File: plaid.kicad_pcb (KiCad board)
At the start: 2 copper layers, 228 x 98 mm, 139 parts, among them J1 USB_OTG, J2 AVR_ISP_6, J3 Conn_01x04, J4 GS2, J5 GS2, SW1 SW_Push, SW10 SW_Push, SW11 SW_Push, SW12 SW_Push, SW13 SW_Push, SW14 SW_Push, SW15 SW_Push, SW16 SW_Push, SW17 SW_Push, SW18 SW_Push, SW19 SW_Push, SW2 SW_Push, SW20 SW_Push, SW21 SW_Push, SW22 SW_Push, SW23 SW_Push, SW24 SW_Push, SW25 SW_Push, SW26 SW_Push, SW27 SW_Push, SW28 SW_Push, SW29 SW_Push, SW3 SW_Push, SW30 SW_Push, SW31 SW_Push, SW32 SW_Push, SW33 SW_Push, SW34 SW_Push, SW35 SW_Push, SW36 SW_Push, SW37 SW_Push, SW38 SW_Push, SW39 SW_Push, SW4 SW_Push, SW40 SW_Push, SW41 SW_Push, SW42 SW_Push, SW43 SW_Push, SW44 SW_Push, SW45 SW_Push, SW46 SW_Push, SW47 SW_Push, SW48 SW_Push, SW49 SW_Push, SW5 SW_Push, SW50 RESET, SW51 BOOT, SW6 SW_Push, SW7 SW_Push, SW8 SW_Push, SW9 SW_Push, U1 ATMEGA328-PU, Y1 16MHz

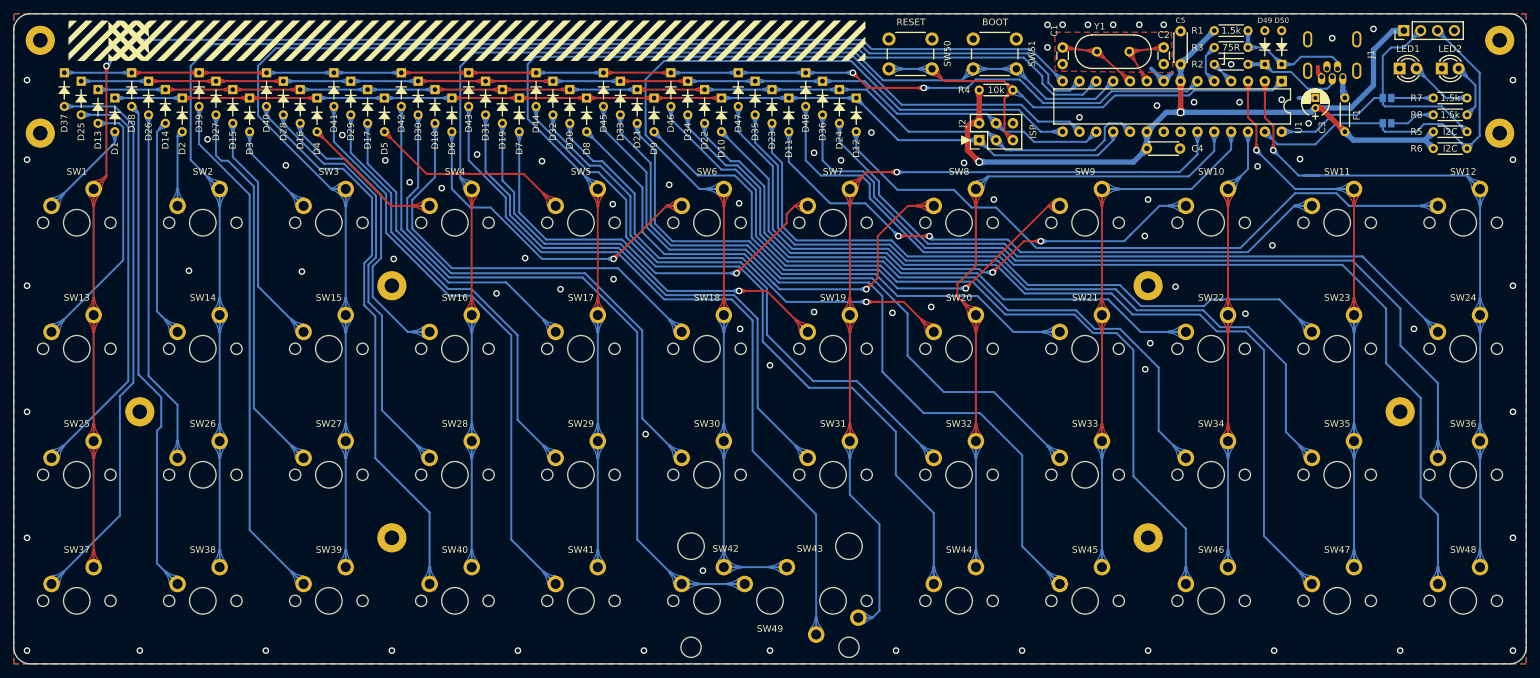
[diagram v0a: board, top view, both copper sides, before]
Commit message: Update PCB to new KiCAD
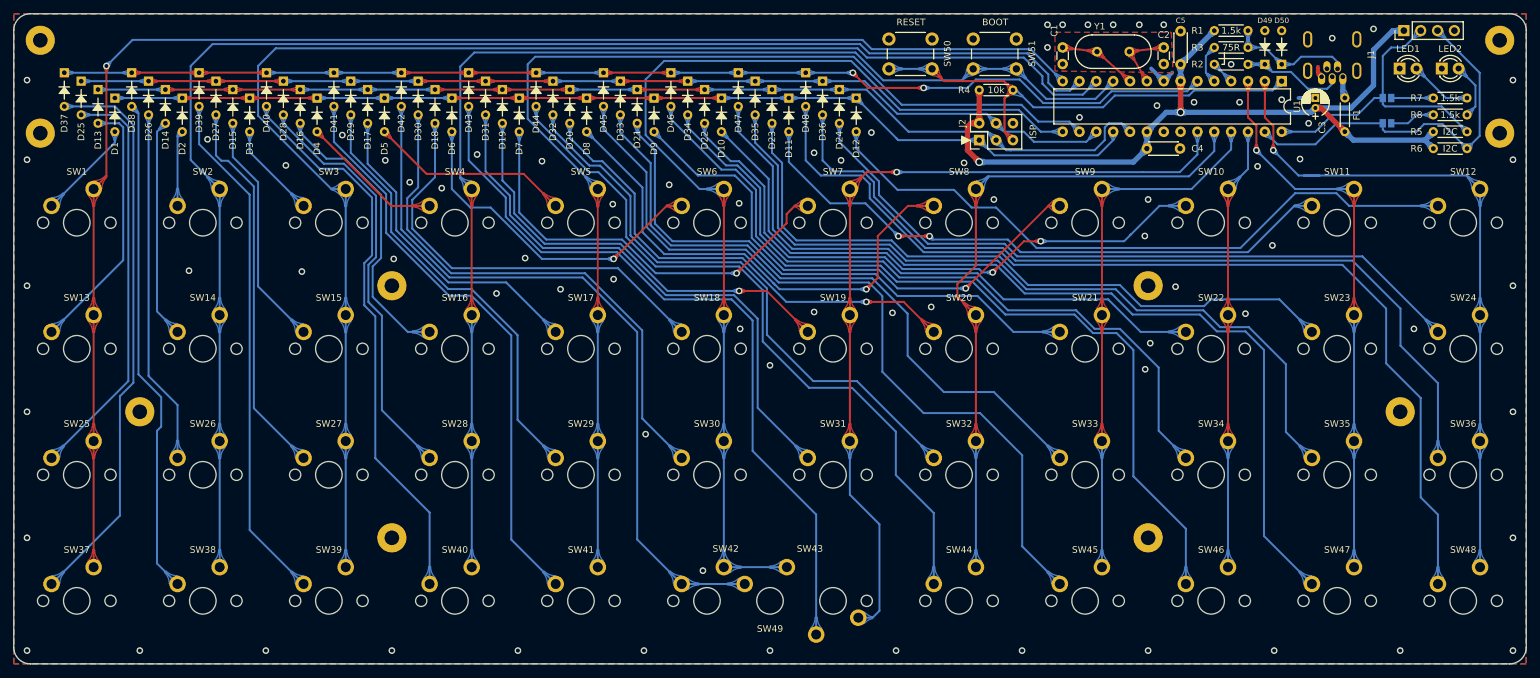
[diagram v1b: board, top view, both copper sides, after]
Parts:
- removed G***: LOGO, plaid_silk:plaid_silk
- removed G***: LOGO, dm9_silks:logo_hsgw_7_5mm
- removed G***: LOGO, dm9_silks:logo_dm9_15mm
- removed G***: LOGO, plaid_silk:plaid_katakana
- removed REF**: Stab_MX_2u, SMKJP:Stab_MX_2u
- C3: value 10u -> 4.7u
- U1: footprint Housings_DIP:DIP-28_W7.62mm -> Package_DIP:DIP-28_W7.62mm
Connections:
- D1 pad 1: /ROW0 -> unconnected-(D1-Pad1)
- D10 pad 1: /ROW0 -> unconnected-(D10-Pad1)
- D11 pad 1: /ROW0 -> unconnected-(D11-Pad1)
- D13 pad 1: /ROW1 -> unconnected-(D13-Pad1)
- D14 pad 1: /ROW1 -> unconnected-(D14-Pad1)
- D15 pad 1: /ROW1 -> unconnected-(D15-Pad1)
- D16 pad 1: /ROW1 -> unconnected-(D16-Pad1)
- D17 pad 1: /ROW1 -> unconnected-(D17-Pad1)
- D18 pad 1: /ROW1 -> unconnected-(D18-Pad1)
- D19 pad 1: /ROW1 -> unconnected-(D19-Pad1)
- D2 pad 1: /ROW0 -> unconnected-(D2-Pad1)
- D20 pad 1: /ROW1 -> unconnected-(D20-Pad1)
- D21 pad 1: /ROW1 -> unconnected-(D21-Pad1)
- D22 pad 1: /ROW1 -> unconnected-(D22-Pad1)
- D23 pad 1: /ROW1 -> unconnected-(D23-Pad1)
- D25 pad 1: /ROW2 -> unconnected-(D25-Pad1)
- D26 pad 1: /ROW2 -> unconnected-(D26-Pad1)
- D27 pad 1: /ROW2 -> unconnected-(D27-Pad1)
- D28 pad 1: /ROW2 -> unconnected-(D28-Pad1)
- D29 pad 1: /ROW2 -> unconnected-(D29-Pad1)
- D3 pad 1: /ROW0 -> unconnected-(D3-Pad1)
- D30 pad 1: /ROW2 -> unconnected-(D30-Pad1)
- D31 pad 1: /ROW2 -> unconnected-(D31-Pad1)
- D32 pad 1: /ROW2 -> unconnected-(D32-Pad1)
- D33 pad 1: /ROW2 -> unconnected-(D33-Pad1)
- D34 pad 1: /ROW2 -> unconnected-(D34-Pad1)
- D35 pad 1: /ROW2 -> unconnected-(D35-Pad1)
- D37 pad 1: /ROW3 -> unconnected-(D37-Pad1)
- D38 pad 1: /ROW3 -> unconnected-(D38-Pad1)
- D39 pad 1: /ROW3 -> unconnected-(D39-Pad1)
- D4 pad 1: /ROW0 -> unconnected-(D4-Pad1)
- D40 pad 1: /ROW3 -> unconnected-(D40-Pad1)
- D41 pad 1: /ROW3 -> unconnected-(D41-Pad1)
- D43 pad 1: /ROW3 -> unconnected-(D43-Pad1)
- D44 pad 1: /ROW3 -> unconnected-(D44-Pad1)
- D45 pad 1: /ROW3 -> unconnected-(D45-Pad1)
- D46 pad 1: /ROW3 -> unconnected-(D46-Pad1)
- D47 pad 1: /ROW3 -> unconnected-(D47-Pad1)
- D5 pad 1: /ROW0 -> unconnected-(D5-Pad1)
- D6 pad 1: /ROW0 -> unconnected-(D6-Pad1)
- D7 pad 1: /ROW0 -> unconnected-(D7-Pad1)
- D8 pad 1: /ROW0 -> unconnected-(D8-Pad1)
- D9 pad 1: /ROW0 -> unconnected-(D9-Pad1)
- J1 pad 4: (no net) -> unconnected-(J1-Pad4)
- J1 pad 6: (no net) -> unconnected-(J1-Pad6)
- U1 pad 21: (no net) -> unconnected-(U1-Pad21)
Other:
- net class Default removed
- net class Power removed

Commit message: Start turning Plaid into Squeezebar
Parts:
- removed D37, D38, D39, D40, D41, D42, D43, D44, D45, D46, D47, D48: 1N4148, dm9_rc:D_DO-35_SOD27_P5.08mm_Horizontal
- removed H10, H3, H4, H5, H6, H7, H8, H9: M2, Mounting_Holes:MountingHole_2.2mm_M2_Pad
- removed LED1: RED, LEDs:LED_D3.0mm
- removed LED2: GREEN, LEDs:LED_D3.0mm
- removed R7, R8: 1.5k, Resistors_THT:R_Axial_DIN0204_L3.6mm_D1.6mm_P5.08mm_Horizontal
- removed SW1, SW10, SW11, SW12, SW13, SW14, SW15, SW16, SW17, SW18, SW19, SW2, SW20, SW21, SW22, SW23, SW24, SW25, SW26, SW27, SW28, SW29, SW3, SW30, SW31, SW32, SW33, SW34, SW35, SW36, SW37, SW38, SW39, SW4, SW40, SW41, SW42, SW43, SW44, SW45, SW46, SW47, SW48, SW5, SW6, SW7, SW8, SW9: SW_Push, SMKJP:SW_Cherry_MX1A_1.00u_PCB
- removed SW49: SW_Push, SMKJP:SW_Cherry_MX1A_2.0U_PCB_universal_center
- added J0: OUTR, Connector_JST:JST_PH_B5B-PH-K_1x05_P2.00mm_Vertical, F.Cu at (168.1, 47.5)
- added J1: PNK, Connector_JST:JST_PH_B5B-PH-K_1x05_P2.00mm_Vertical, F.Cu at (175.7, 47.5)
- added J10: I2C, Connector_JST:JST_PH_B5B-PH-K_1x05_P2.00mm_Vertical, F.Cu at (244.3, 47.5)
- added J13: AudioJack4, Connector_Audio:Jack_3.5mm_PJ320E_Horizontal, F.Cu at (304.3, 15.7)
- added J14: RGB, Connector_PinSocket_2.54mm:PinSocket_1x03_P2.54mm_Vertical, F.Cu at (325.0, 60.6)
- added J2: RNG, Connector_JST:JST_PH_B5B-PH-K_1x05_P2.00mm_Vertical, F.Cu at (183.3, 47.5)
- added J3: MID, Connector_JST:JST_PH_B5B-PH-K_1x05_P2.00mm_Vertical, F.Cu at (191.0, 47.5)
- added J6: THM1, Connector_JST:JST_PH_B5B-PH-K_1x05_P2.00mm_Vertical, F.Cu at (213.8, 47.5)
- added J7: THM2, Connector_JST:JST_PH_B5B-PH-K_1x05_P2.00mm_Vertical, F.Cu at (221.4, 47.5)
- added J8: ENC, Connector_JST:JST_PH_B5B-PH-K_1x05_P2.00mm_Vertical, F.Cu at (229.1, 47.5)
- added J9: I2C, Connector_JST:JST_PH_B5B-PH-K_1x05_P2.00mm_Vertical, F.Cu at (236.7, 47.5)
- added JP1: A0, Jumper:SolderJumper-3_P1.3mm_Bridged12_Pad1.0x1.5mm, F.Cu at (312.0, 71.1)
- added JP2: A1, Jumper:SolderJumper-3_P1.3mm_Bridged12_Pad1.0x1.5mm, F.Cu at (300.7, 71.0)
- added JP3: A2, Jumper:SolderJumper-3_P1.3mm_Bridged12_Pad1.0x1.5mm, F.Cu at (306.3, 71.1)
- added U2: MCP23017_SP, Package_DIP:DIP-28_W7.62mm, F.Cu at (264.6, 28.4)
- D33, D34, D35, D36: value 1N4148 -> WS2812B; footprint dm9_rc:D_DO-35_SOD27_P5.08mm_Horizontal -> LED_SMD:LED_WS2812B_PLCC4_5.0x5.0mm_P3.2mm
- H1, H2: value M2 -> M3; footprint Mounting_Holes:MountingHole_2.2mm_M2_Pad -> MountingHole:MountingHole_3.2mm_M3
- J4: value GS2 -> IDX; footprint Connectors:GS2 -> Connector_JST:JST_PH_B5B-PH-K_1x05_P2.00mm_Vertical; moved to F.Cu
- J5: value GS2 -> INNR; footprint Connectors:GS2 -> Connector_JST:JST_PH_B5B-PH-K_1x05_P2.00mm_Vertical; moved to F.Cu
- moved H1 218.7 mm to (272.2, 39.8)
- moved D33 199.5 mm to (340.8, 55.1), turned to 0 degrees
- moved D34 189.8 mm to (340.8, 48.5), turned to 0 degrees
- moved D36 185.9 mm to (356.7, 41.9), turned to 0 degrees
- moved D35 169.7 mm to (331.5, 61.6), turned to 0 degrees
- moved H2 122.4 mm to (169.4, 27.1)
- moved D1 117.7 mm to (177.0, 28.4)
- moved D2 110.0 mm to (179.5, 29.7)
- moved D3 102.4 mm to (182.1, 30.9)
- moved D4 87.5 mm to (174.5, 27.1)
- moved J4 60.4 mm to (198.6, 47.5)
- moved J5 54.3 mm to (206.2, 47.5)
- moved U1 41.6 mm to (264.6, 25.9)
- moved J15 35.7 mm to (272.2, 32.6)
- moved C4 28.6 mm to (249.4, 71.6)
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- renumbered J3 to J11, J2 to J12, J1 to J15
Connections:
- D1 pad 1: unconnected-(D1-Pad1) -> Net-(D1-Pad1)
- D1 pad 2: Net-(D1-Pad2) -> /ROW0
- D10 pad 1: unconnected-(D10-Pad1) -> Net-(D10-Pad1)
- D10 pad 2: Net-(D10-Pad2) -> /ROW1
- D11 pad 1: unconnected-(D11-Pad1) -> Net-(D11-Pad1)
- D11 pad 2: Net-(D11-Pad2) -> /ROW2
- D12 pad 1: /ROW0 -> Net-(D12-Pad1)
- D12 pad 2: Net-(D12-Pad2) -> /ROW3
- D13 pad 1: unconnected-(D13-Pad1) -> Net-(D13-Pad1)
- D13 pad 2: Net-(D13-Pad2) -> /ROW0
- D14 pad 1: unconnected-(D14-Pad1) -> Net-(D14-Pad1)
- D14 pad 2: Net-(D14-Pad2) -> /ROW1
- D15 pad 1: unconnected-(D15-Pad1) -> Net-(D15-Pad1)
- D15 pad 2: Net-(D15-Pad2) -> /ROW2
- D16 pad 1: unconnected-(D16-Pad1) -> Net-(D16-Pad1)
- D16 pad 2: Net-(D16-Pad2) -> /ROW3
- D17 pad 1: unconnected-(D17-Pad1) -> Net-(D17-Pad1)
- D17 pad 2: Net-(D17-Pad2) -> /ROW0
- D18 pad 1: unconnected-(D18-Pad1) -> Net-(D18-Pad1)
- D18 pad 2: Net-(D18-Pad2) -> /ROW1
- D19 pad 1: unconnected-(D19-Pad1) -> Net-(D19-Pad1)
- D19 pad 2: Net-(D19-Pad2) -> /ROW2
- D2 pad 1: unconnected-(D2-Pad1) -> Net-(D2-Pad1)
- D2 pad 2: Net-(D2-Pad2) -> /ROW1
- D20 pad 1: unconnected-(D20-Pad1) -> Net-(D20-Pad1)
- D20 pad 2: Net-(D20-Pad2) -> /ROW3
- D21 pad 1: unconnected-(D21-Pad1) -> Net-(D21-Pad1)
- D21 pad 2: Net-(D21-Pad2) -> /ROW0
- D22 pad 1: unconnected-(D22-Pad1) -> Net-(D22-Pad1)
- D22 pad 2: Net-(D22-Pad2) -> /ROW1
- D23 pad 1: unconnected-(D23-Pad1) -> Net-(D23-Pad1)
- D23 pad 2: Net-(D23-Pad2) -> /ROW2
- D24 pad 1: /ROW1 -> Net-(D24-Pad1)
- D24 pad 2: Net-(D24-Pad2) -> /ROW3
- D25 pad 1: unconnected-(D25-Pad1) -> Net-(D25-Pad1)
- D25 pad 2: Net-(D25-Pad2) -> /ROW0
- D26 pad 1: unconnected-(D26-Pad1) -> Net-(D26-Pad1)
- D26 pad 2: Net-(D26-Pad2) -> /ROW1
- D27 pad 1: unconnected-(D27-Pad1) -> Net-(D27-Pad1)
- D27 pad 2: Net-(D27-Pad2) -> /ROW2
- D28 pad 1: unconnected-(D28-Pad1) -> Net-(D28-Pad1)
- D28 pad 2: Net-(D28-Pad2) -> /ROW3
- D29 pad 1: unconnected-(D29-Pad1) -> Net-(D29-Pad1)
- D29 pad 2: Net-(D29-Pad2) -> /ROW0
- D3 pad 1: unconnected-(D3-Pad1) -> Net-(D3-Pad1)
- D3 pad 2: Net-(D3-Pad2) -> /ROW2
- D30 pad 1: unconnected-(D30-Pad1) -> Net-(D30-Pad1)
- D30 pad 2: Net-(D30-Pad2) -> /ROW1
- D31 pad 1: unconnected-(D31-Pad1) -> Net-(D31-Pad1)
- D31 pad 2: Net-(D31-Pad2) -> /ROW2
- D32 pad 1: unconnected-(D32-Pad1) -> Net-(D32-Pad1)
- D32 pad 2: Net-(D32-Pad2) -> /ROW3
- D33 pad 1: unconnected-(D33-Pad1) -> +5V
- D33 pad 2: Net-(D33-Pad2) -> unconnected-(D33-Pad2)
- D34 pad 1: unconnected-(D34-Pad1) -> +5V
- D34 pad 2: Net-(D34-Pad2) -> unconnected-(D34-Pad2)
- D35 pad 1: unconnected-(D35-Pad1) -> +5V
- D35 pad 2: Net-(D35-Pad2) -> unconnected-(D35-Pad2)
- D36 pad 1: /ROW2 -> +5V
- D36 pad 2: Net-(D36-Pad2) -> /RGB_OUT
- D4 pad 1: unconnected-(D4-Pad1) -> Net-(D4-Pad1)
- D4 pad 2: Net-(D4-Pad2) -> /ROW3
- D5 pad 1: unconnected-(D5-Pad1) -> Net-(D5-Pad1)
- D5 pad 2: Net-(D5-Pad2) -> /ROW0
- D6 pad 1: unconnected-(D6-Pad1) -> Net-(D6-Pad1)
- D6 pad 2: Net-(D6-Pad2) -> /ROW1
- D7 pad 1: unconnected-(D7-Pad1) -> Net-(D7-Pad1)
- D7 pad 2: Net-(D7-Pad2) -> /ROW2
- D8 pad 1: unconnected-(D8-Pad1) -> Net-(D8-Pad1)
- D8 pad 2: Net-(D8-Pad2) -> /ROW3
- D9 pad 1: unconnected-(D9-Pad1) -> Net-(D9-Pad1)
- D9 pad 2: Net-(D9-Pad2) -> /ROW0
- J12 pad 1: /ROW0 -> /ROW2
- J12 pad 4: /ROW2 -> /ROW3
- J4 pad 1: Net-(J4-Pad1) -> /COL4
- J4 pad 2: /i2c_SCL -> Net-(D17-Pad1)
- J5 pad 1: Net-(J5-Pad1) -> /COL5
- J5 pad 2: /i2c_SDA -> Net-(D21-Pad1)
- SW51 pad 1: /COL3 -> /BOOT
- U1 pad 11: /COL3 -> /BOOT
- U1 pad 17: /ROW2 -> /ROW3
- U1 pad 18: /ROW0 -> /ROW2
- U1 pad 2: /COL11 -> /ROW0
- U1 pad 25: /COL8 -> /E1
- U1 pad 26: /COL9 -> /E2
- U1 pad 3: /COL10 -> /COL3
- U1 pad 6: /ROW3 -> /RGB
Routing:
- net /COL0: track 224.7 -> 0.00 mm, vias 1 -> 0
- net /COL1: track 217.0 -> 0.00 mm
- net /COL2: track 214.2 -> 0.00 mm
- net /COL3: track 180.9 -> 0.00 mm
- net /ROW3: track 175.6 -> 0.00 mm, vias 2 -> 0
- net /COL4: track 168.5 -> 0.00 mm
- net /ROW1: track 162.9 -> 0.00 mm
- net /COL5: track 158.5 -> 0.00 mm
- net /ROW2: track 157.5 -> 0.00 mm
- net /ROW0: track 156.3 -> 0.00 mm
- net Net-(D48-Pad2): track 150.9 -> 0.00 mm
- net Net-(D47-Pad2): track 140.5 -> 0.00 mm
- net Net-(D36-Pad2): track 129.4 -> 0.00 mm
- net Net-(D46-Pad2): track 128.7 -> 0.00 mm
- net +5V: track 127.6 -> 0.00 mm, vias 2 -> 0
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- removed copper zone on B.Cu, net GND
- removed copper zone on F.Cu, net GND
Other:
- board size 228 x 98 mm -> 110.5 x 26.7 mm

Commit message: Route a Squeezebar
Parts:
- removed D1, D10, D11, D12, D13, D14, D15, D16, D17, D18, D19, D2, D20, D21, D22, D23, D24, D25, D26, D27, D28, D29, D3, D30, D31, D32, D4, D5, D6, D7, D8, D9: 1N4148, dm9_rc:D_DO-35_SOD27_P5.08mm_Horizontal
- removed D33, D34, D35, D36: WS2812B, LED_SMD:LED_WS2812B_PLCC4_5.0x5.0mm_P3.2mm
- removed J12: AVR_ISP_6, Pin_Headers:Pin_Header_Straight_2x03_Pitch2.54mm
- removed J13: AudioJack4, Connector_Audio:Jack_3.5mm_PJ320E_Horizontal
- removed JP1: A0, Jumper:SolderJumper-3_P1.3mm_Bridged12_Pad1.0x1.5mm
- removed JP2: A1, Jumper:SolderJumper-3_P1.3mm_Bridged12_Pad1.0x1.5mm
- removed JP3: A2, Jumper:SolderJumper-3_P1.3mm_Bridged12_Pad1.0x1.5mm
- H1, H2: value M3 -> M2; footprint MountingHole:MountingHole_3.2mm_M3 -> MountingHole:MountingHole_2.2mm_M2
- moved J14 266.1 mm to (58.9, 57.1), turned to 180 degrees
- moved U1 134.0 mm to (135.1, 60.2)
- moved U2 134.0 mm to (135.1, 62.7)
- moved SW51 132.1 mm to (69.0, 56.6)
- moved J7 126.4 mm to (97.0, 69.4)
- moved J6 125.1 mm to (90.6, 69.4)
- moved R5 124.7 mm to (140.3, 51.9), turned to -90 degrees
- moved J5 123.9 mm to (84.3, 69.4)
- moved J4 122.6 mm to (77.9, 69.4)
- moved R6 122.6 mm to (142.8, 51.9), turned to -90 degrees
- moved J3 121.4 mm to (71.6, 69.4)
- moved J2 120.1 mm to (65.2, 69.4)
- moved H2 119.1 mm to (53.2, 53.2)
- moved J1 118.9 mm to (58.9, 69.4)
- moved J0 117.6 mm to (52.5, 69.4)
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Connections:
- J0 pad 2: Net-(D1-Pad1) -> /ROW0
- J0 pad 3: Net-(D2-Pad1) -> /ROW1
- J0 pad 4: Net-(D3-Pad1) -> /ROW2
- J0 pad 5: Net-(D4-Pad1) -> /ROW3
- J1 pad 2: Net-(D5-Pad1) -> /ROW0
- J1 pad 3: Net-(D6-Pad1) -> /ROW1
- J1 pad 4: Net-(D7-Pad1) -> /ROW2
- J1 pad 5: Net-(D8-Pad1) -> /ROW3
- J10 pad 2: /i2c_SDA -> /INT
- J10 pad 3: /i2c_SCL -> /i2c_SDA
- J10 pad 4: /INT -> /i2c_SCL
- J11 pad 2: /i2c_SCL -> /i2c_SDA
- J11 pad 3: /i2c_SDA -> /i2c_SCL
- J14 pad 2: /RGB_OUT -> /RGB
- J2 pad 2: Net-(D9-Pad1) -> /ROW0
- J2 pad 3: Net-(D10-Pad1) -> /ROW1
- J2 pad 4: Net-(D11-Pad1) -> /ROW2
- J2 pad 5: Net-(D12-Pad1) -> /ROW3
- J3 pad 2: Net-(D13-Pad1) -> /ROW0
- J3 pad 3: Net-(D14-Pad1) -> /ROW1
- J3 pad 4: Net-(D15-Pad1) -> /ROW2
- J3 pad 5: Net-(D16-Pad1) -> /ROW3
- J4 pad 2: Net-(D17-Pad1) -> /ROW0
- J4 pad 3: Net-(D18-Pad1) -> /ROW1
- J4 pad 4: Net-(D19-Pad1) -> /ROW2
- J4 pad 5: Net-(D20-Pad1) -> /ROW3
- J5 pad 2: Net-(D21-Pad1) -> /ROW0
- J5 pad 3: Net-(D22-Pad1) -> /ROW1
- J5 pad 4: Net-(D23-Pad1) -> /ROW2
- J5 pad 5: Net-(D24-Pad1) -> /ROW3
- J6 pad 2: Net-(D25-Pad1) -> /ROW0
- J6 pad 3: Net-(D26-Pad1) -> /ROW1
- J6 pad 4: Net-(D27-Pad1) -> /ROW2
- J6 pad 5: Net-(D28-Pad1) -> /ROW3
- J7 pad 2: Net-(D29-Pad1) -> /ROW0
- J7 pad 3: Net-(D30-Pad1) -> /ROW1
- J7 pad 4: Net-(D31-Pad1) -> /ROW2
- J7 pad 5: Net-(D32-Pad1) -> /ROW3
- J8 pad 1: GND -> /E2
- J8 pad 2: /BOOT -> GND
- J8 pad 4: GND -> /ROW3
- J8 pad 5: /E2 -> /COL0
- J9 pad 2: /i2c_SDA -> /INT
- J9 pad 3: /i2c_SCL -> /i2c_SDA
- J9 pad 4: /INT -> /i2c_SCL
- R5 pad 2: /i2c_SCL -> /i2c_SDA
- R6 pad 2: /i2c_SDA -> /i2c_SCL
- SW51 pad 1: /BOOT -> /COL0
- U1 pad 11: /BOOT -> /COL0
- U1 pad 12: /COL2 -> /COL3
- U1 pad 13: /COL1 -> /RGB
- U1 pad 14: /COL0 -> /COL7
- U1 pad 17: /ROW3 -> /INT
- U1 pad 18: /ROW2 -> /ROW0
- U1 pad 2: /ROW0 -> /COL1
- U1 pad 23: /COL6 -> /ROW2
- U1 pad 24: /COL7 -> /ROW3
- U1 pad 3: /COL3 -> /COL2
- U1 pad 6: /RGB -> /COL6
- U2 pad 15: /A2 -> +5V
- U2 pad 16: /A1 -> +5V
- U2 pad 17: /A0 -> +5V
- U2 pad 19: /INT -> unconnected-(U2-Pad19)
- U2 pad 20: unconnected-(U2-Pad20) -> /INT
- U2 pad 28: /BOOT -> unconnected-(U2-Pad28)
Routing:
- net +5V: track 0.00 -> 218.1 mm, vias 0 -> 2
- net GND: track 0.00 -> 197.7 mm, vias 0 -> 1
- net /COL0: track 0.00 -> 107.9 mm, vias 0 -> 1
- net /ROW3: track 0.00 -> 93.8 mm
- net /COL1: track 0.00 -> 93.4 mm
- net /COL4: track 0.00 -> 88.8 mm
- net /RESET: track 0.00 -> 88.5 mm
- net /ROW2: track 0.00 -> 77.0 mm
- net /i2c_SDA: track 0.00 -> 76.5 mm
- net /COL2: track 0.00 -> 76.3 mm
- net /ROW1: track 0.00 -> 71.2 mm, vias 0 -> 1
- net /i2c_SCL: track 0.00 -> 70.8 mm
- net /COL5: track 0.00 -> 70.1 mm
- net /ROW0: track 0.00 -> 68.4 mm
- net /RGB: track 0.00 -> 64.0 mm
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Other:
- board size 110.5 x 26.7 mm -> 117.5 x 21 mm
- board text removed: "5V"
- board text removed: "BOOT"
- board text removed: "GND"
- board text removed: "ISP"
- board text removed: "LED"
- board text removed: "RESET"
- board text removed: "SCL"
- board text removed: "SDA"
